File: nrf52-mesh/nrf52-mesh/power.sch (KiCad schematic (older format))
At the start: 8 parts

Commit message: continue nRF52 power
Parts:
- added C? (x6): C, symbol Device:C
- added L? (x2): L, symbol Device:L
- added R? (x6): R, symbol Device:R
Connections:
- net +3V3: now also C?.1, L?.1, R?.1
- net GND: now also U?.2 (GND), U?.2 (GND), C?.2, C?.2, C?.2, C?.2, C?.2, C?.2, R?.2, R?.2, R?.2
- net at U?.1 (EN): now also R?.1, R?.2
- net at U?.3 (PH): now also L?.2
- net +15V: now reaches U?.4 (VIN)
- net +15V: now also C?.1, C?.1, R?.1
- net at U?.5 (FB): now also R?.1, R?.2 (x2)
- net +5V: now reaches U?.1 (EN)
- net +5V: now also U?.4 (VIN), C?.1, C?.1, C?.1, L?.1, R?.1
- net at U?.3 (SW): now also L?.2
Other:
- moved on the sheet: U?

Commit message: next portion
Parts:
- removed U?: CP2102N-A01-GQFN24, Package_DFN_QFN:QFN-24-1EP_4x4mm_P0.5mm_EP2.6x2.6mm, symbol Interface_USB:CP2102N-A01-GQFN24
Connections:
- net GND: now also U?.6 (GND)
- net LEDREGEN: now reaches U?.3 (EN)
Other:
- moved on the sheet: U?
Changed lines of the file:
@@
 $Descr A4 11693 8268
 encoding utf-8
-Sheet 2 7
+Sheet 2 8
 Title ""
 Date ""
@@
 	5400 3450 5400 650
 $Comp
-L Interface_USB:CP2102N-A01-GQFN24 U?
-U 1 1 5E5187FA
-P 5700 5000
-F 0 "U?" H 5700 6081 50  0000 C CNN
-F 1 "CP2102N-A01-GQFN24" H 5700 5990 50  0000 C CNN
-F 2 "Package_DFN_QFN:QFN-24-1EP_4x4mm_P0.5mm_EP2.6x2.6mm" H 6150 4200 50  0001 L CNN
-F 3 "https://www.silabs.com/documents/public/data-sheets/cp2102n-datasheet.pdf" H 5750 3950 50  0001 C CNN
-	1    5700 5000
-	1    0    0    -1
-$EndComp
-$Comp
 L Regulator_Switching:TPS560200 U?
 U 1 1 5E51A6D3
@@
 L kilib:FAN5341 U?
 U 1 1 5E51BD5F
-P 4100 6900
-F 0 "U?" H 4100 7381 50  0000 C CNN
-F 1 "FAN5341" H 4100 7290 50  0000 C CNN
-F 2 "kifootp:FAN5341" H 4150 6650 50  0001 L CNN
-F 3 "" H 4100 6900 50  0001 C CNN
-	1    4100 6900
+P 4800 5400
+F 0 "U?" H 4800 5881 50  0000 C CNN
+F 1 "FAN5341" H 4800 5790 50  0000 C CNN
+F 2 "kifootp:FAN5341" H 4850 5150 50  0001 L CNN
+F 3 "" H 4800 5400 50  0001 C CNN
+	1    4800 5400
 	1    0    0    -1
 $EndComp
@@
 Wire Wire Line
 	3150 6650 3200 6650
+Text GLabel 3650 5400 0    50   Input ~ 0
+LEDREGEN
+Wire Wire Line
+	3650 5400 4400 5400
+$Comp
+L power:GND #PWR?
+U 1 1 5E59FA50
+P 4800 6050
+F 0 "#PWR?" H 4800 5800 50  0001 C CNN
+F 1 "GND" H 4805 5877 50  0000 C CNN
+F 2 "" H 4800 6050 50  0001 C CNN
+F 3 "" H 4800 6050 50  0001 C CNN
+	1    4800 6050
+	1    0    0    -1
+$EndComp
+Wire Wire Line
+	4800 5700 4800 6050
 $EndSCHEMATC

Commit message: next portion
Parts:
- added C? (x2): C, symbol pspice:C
- added L?: L, symbol Device:L
- added R? (x2): R, symbol Device:R
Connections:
- net +3V3: now also U?.2 (VIN), C?.1, L?.1, R?.1
- net +5V: now also U?.5 (BAT)
- net GND: now also C?.2, C?.2, R?.2
- net CHARGE: now reaches U?.3 (CHG#)
- net CHARGE: now also R?.2
- net LEDIN: now reaches U?.1 (VOUT)
- net LEDIN: now also C?.1
- net LEDOUT: now reaches U?.4 (FB)
- net LEDOUT: now also R?.1
- net at U?.5 (SW): now also L?.2
- no-connect marks 0 -> 1
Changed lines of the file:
@@
 Wire Wire Line
 	4800 5700 4800 6050
+$Comp
+L pspice:C C?
+U 1 1 5E5B5AAA
+P 5900 5900
+F 0 "C?" H 6078 5946 50  0000 L CNN
+F 1 "C" H 6078 5855 50  0000 L CNN
+F 2 "" H 5900 5900 50  0001 C CNN
+F 3 "~" H 5900 5900 50  0001 C CNN
+	1    5900 5900
+	1    0    0    -1
+$EndComp
+$Comp
+L Device:R R?
+U 1 1 5E5B6411
+P 5450 5800
+F 0 "R?" H 5520 5846 50  0000 L CNN
+F 1 "R" H 5520 5755 50  0000 L CNN
+F 2 "" V 5380 5800 50  0001 C CNN
+F 3 "~" H 5450 5800 50  0001 C CNN
+	1    5450 5800
+	1    0    0    -1
+$EndComp
+Text GLabel 6200 5400 2    50   Input ~ 0
+LEDIN
+Text GLabel 6200 5500 2    50   Input ~ 0
+LEDOUT
+Wire Wire Line
+	5200 5500 5450 5500
+Wire Wire Line
+	6200 5400 5900 5400
+Wire Wire Line
+	5450 5500 5450 5650
+Connection ~ 5450 5500
+$Comp
+L power:GND #PWR?
+U 1 1 5E5C1EAB
+P 5450 6300
+F 0 "#PWR?" H 5450 6050 50  0001 C CNN
+F 1 "GND" H 5455 6127 50  0000 C CNN
+F 2 "" H 5450 6300 50  0001 C CNN
+F 3 "" H 5450 6300 50  0001 C CNN
+	1    5450 6300
+	1    0    0    -1
+$EndComp
+Wire Wire Line
+	5450 5950 5450 6300
+$Comp
+L power:GND #PWR?
+U 1 1 5E5C3E72
+P 5900 6500
+F 0 "#PWR?" H 5900 6250 50  0001 C CNN
+F 1 "GND" H 5905 6327 50  0000 C CNN
+F 2 "" H 5900 6500 50  0001 C CNN
+F 3 "" H 5900 6500 50  0001 C CNN
+	1    5900 6500
+	1    0    0    -1
+$EndComp
+Wire Wire Line
+	5900 6150 5900 6500
+Wire Wire Line
+	5450 5500 6200 5500
+Wire Wire Line
+	5900 5650 5900 5400
+Connection ~ 5900 5400
+Wire Wire Line
+	5900 5400 5200 5400
+$Comp
+L pspice:C C?
+U 1 1 5E5C88CC
+P 4100 4500
+F 0 "C?" H 4278 4546 50  0000 L CNN
+F 1 "C" H 4278 4455 50  0000 L CNN
+F 2 "" H 4100 4500 50  0001 C CNN
+F 3 "~" H 4100 4500 50  0001 C CNN
+	1    4100 4500
+	1    0    0    -1
+$EndComp
+$Comp
+L Device:L L?
+U 1 1 5E5C902A
+P 5450 4850
+F 0 "L?" H 5503 4896 50  0000 L CNN
+F 1 "L" H 5503 4805 50  0000 L CNN
+F 2 "" H 5450 4850 50  0001 C CNN
+F 3 "~" H 5450 4850 50  0001 C CNN
+	1    5450 4850
+	1    0    0    -1
+$EndComp
+$Comp
+L power:GND #PWR?
+U 1 1 5E5C97A4
+P 4100 5100
+F 0 "#PWR?" H 4100 4850 50  0001 C CNN
+F 1 "GND" H 4105 4927 50  0000 C CNN
+F 2 "" H 4100 5100 50  0001 C CNN
+F 3 "" H 4100 5100 50  0001 C CNN
+	1    4100 5100
+	1    0    0    -1
+$EndComp
+Wire Wire Line
+	4100 4750 4100 5100
+Wire Wire Line
+	4800 5100 4800 4300
+Wire Wire Line
+	4800 3900 4100 3900
+Wire Wire Line
+	4100 3900 4100 4250
+Wire Wire Line
+	5450 4700 5450 4300
+Wire Wire Line
+	5450 4300 4800 4300
+Connection ~ 4800 4300
+Wire Wire Line
+	4800 4300 4800 3900
+$Comp
+L power:+3V3 #PWR?
+U 1 1 5E5D1C7A
+P 4800 3700
+AR Path="/5E5D1C7A" Ref="#PWR?"  Part="1"
+AR Path="/5E4CCB9A/5E5D1C7A" Ref="#PWR?"  Part="1"
+F 0 "#PWR?" H 4800 3550 50  0001 C CNN
+F 1 "+3V3" H 4815 3873 50  0000 C CNN
+F 2 "" H 4800 3700 50  0001 C CNN
+F 3 "" H 4800 3700 50  0001 C CNN
+	1    4800 3700
+	1    0    0    -1
+$EndComp
+Wire Wire Line
+	4800 3700 4800 3900
+Connection ~ 4800 3900
+Wire Wire Line
+	5200 5300 5450 5300
+Wire Wire Line
+	5450 5300 5450 5000
+$Comp
+L power:+5V #PWR?
+U 1 1 5E5DDB7A
+P 2950 4050
+F 0 "#PWR?" H 2950 3900 50  0001 C CNN
+F 1 "+5V" H 2965 4223 50  0000 C CNN
+F 2 "" H 2950 4050 50  0001 C CNN
+F 3 "" H 2950 4050 50  0001 C CNN
+	1    2950 4050
+	1    0    0    -1
+$EndComp
+Wire Wire Line
+	2200 4500 2950 4500
+Wire Wire Line
+	2950 4500 2950 4050
+$Comp
+L power:+3V3 #PWR?
+U 1 1 5E5E538B
+P 3350 4050
+AR Path="/5E5E538B" Ref="#PWR?"  Part="1"
+AR Path="/5E4CCB9A/5E5E538B" Ref="#PWR?"  Part="1"
+F 0 "#PWR?" H 3350 3900 50  0001 C CNN
+F 1 "+3V3" H 3365 4223 50  0000 C CNN
+F 2 "" H 3350 4050 50  0001 C CNN
+F 3 "" H 3350 4050 50  0001 C CNN
+	1    3350 4050
+	1    0    0    -1
+$EndComp
+$Comp
+L Device:R R?
+U 1 1 5E5E8405
+P 3350 4450
+F 0 "R?" H 3420 4496 50  0000 L CNN
+F 1 "R" H 3420 4405 50  0000 L CNN
+F 2 "" V 3280 4450 50  0001 C CNN
+F 3 "~" H 3350 4450 50  0001 C CNN
+	1    3350 4450
+	1    0    0    -1
+$EndComp
+Wire Wire Line
+	3350 4050 3350 4300
+Wire Wire Line
+	3350 4800 3350 4600
+Text GLabel 2950 5050 2    50   Input ~ 0
+CHARGE
+Wire Wire Line
+	2500 4800 2500 5050
+Wire Wire Line
+	2500 5050 2950 5050
+Wire Wire Line
+	2200 4800 2500 4800
+Connection ~ 2500 4800
+Wire Wire Line
+	2500 4800 3350 4800
+NoConn ~ 1400 4800
 $EndSCHEMATC

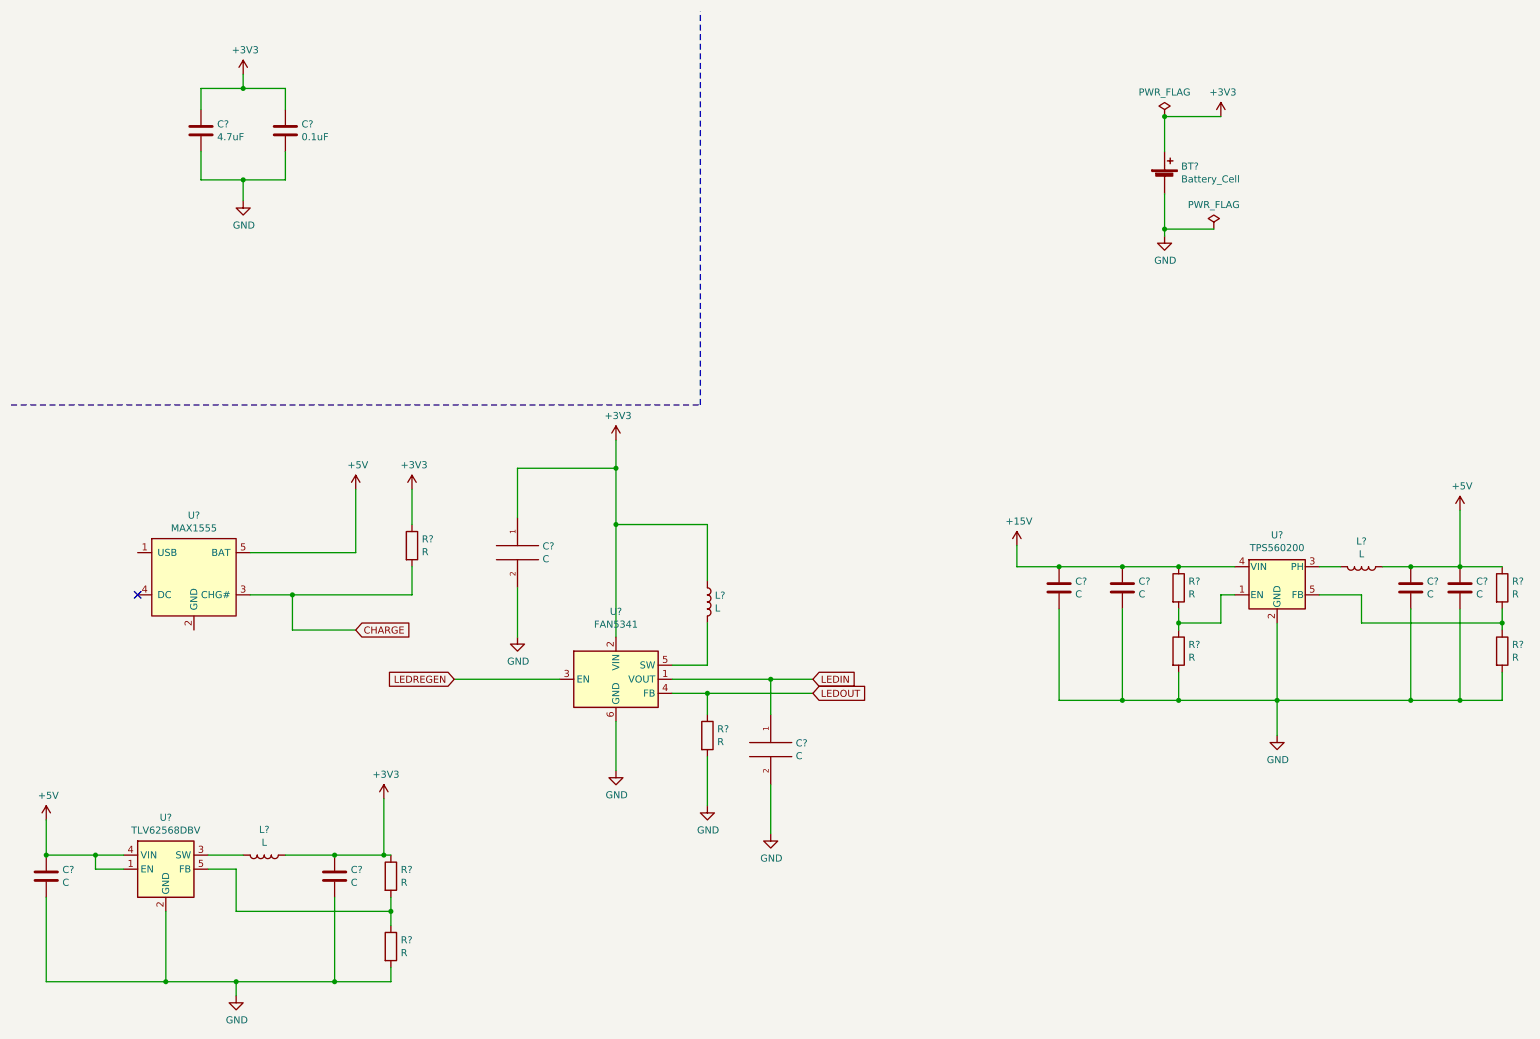
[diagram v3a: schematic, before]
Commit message: CP2102N + MAX1555 + FAN5341 + TPS560200 + TLV62568
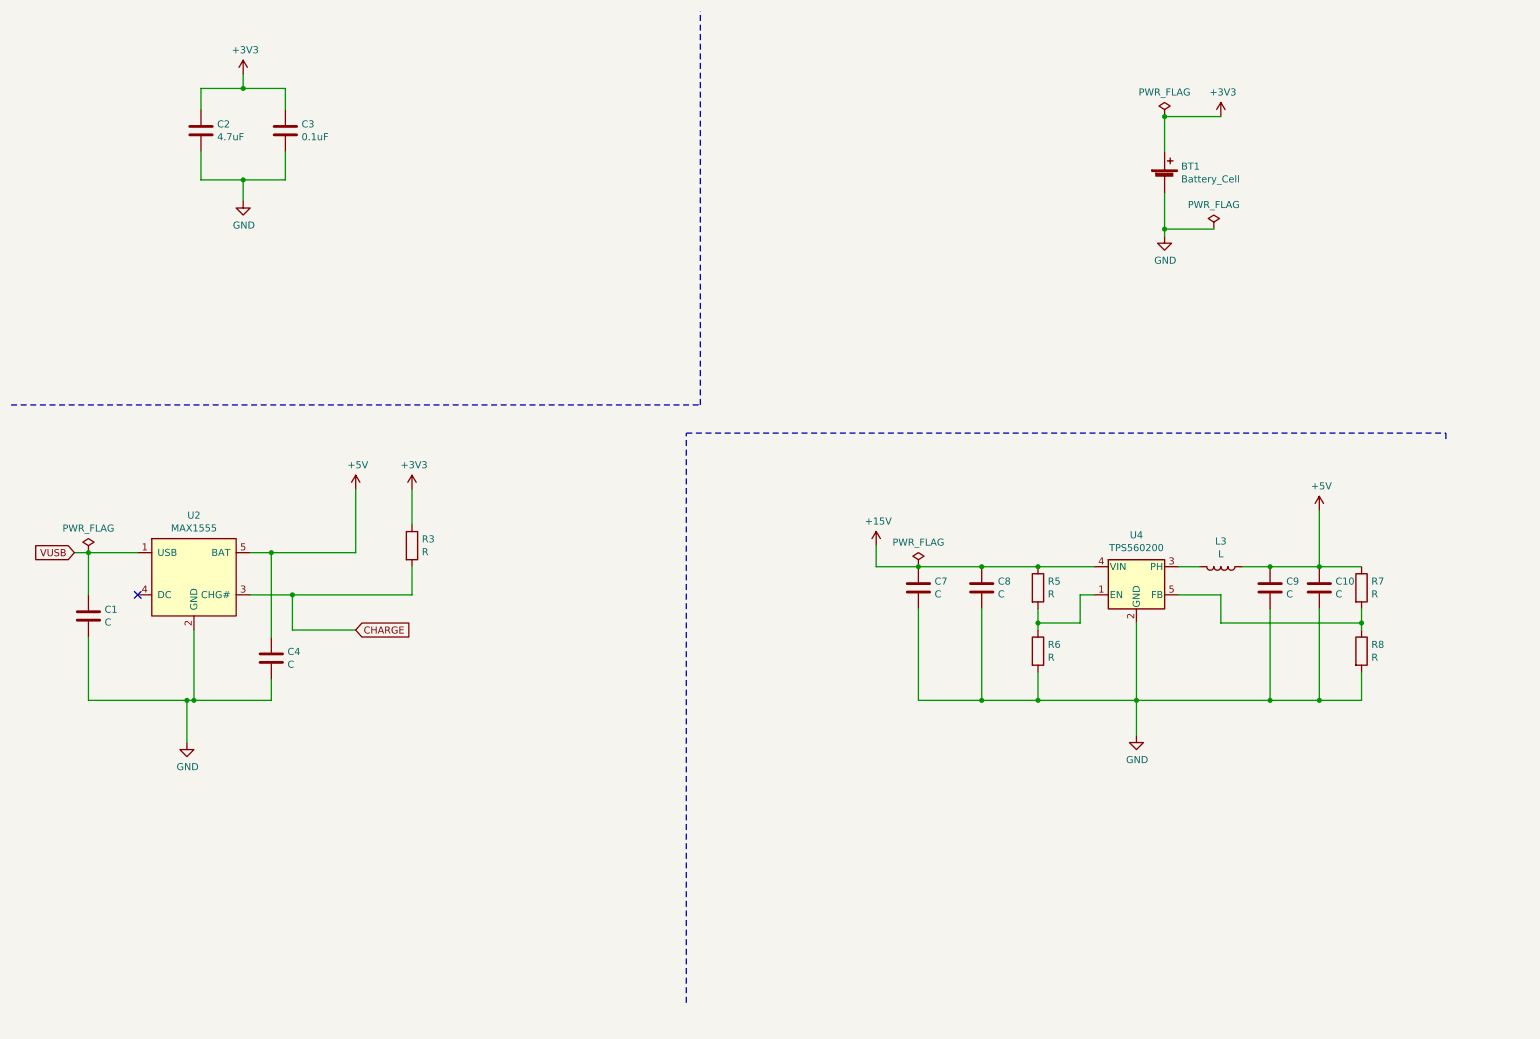
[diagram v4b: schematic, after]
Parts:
- removed C? (x2): C, symbol Device:C
- removed C? (x2): C, symbol pspice:C
- removed L? (x2): L, symbol Device:L
- removed R? (x3): R, symbol Device:R
- removed U?: TLV62568DBV, Package_TO_SOT_SMD:SOT-23-5, symbol Regulator_Switching:TLV62568DBV
- removed U?: FAN5341, kifootp:FAN5341, symbol kilib:FAN5341
- added C1, C4: C, symbol Device:C
- gave numbers to parts that had none: 15
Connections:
- net +5V: now also C4.2
- net GND: now also U2.2 (GND), C1.2, C4.1
- net VUSB: now reaches U2.1 (USB)
- net VUSB: now also C1.1
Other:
- moved on the sheet: C10, C7, C8, C9, L3, R5, R6, R7, R8, U4

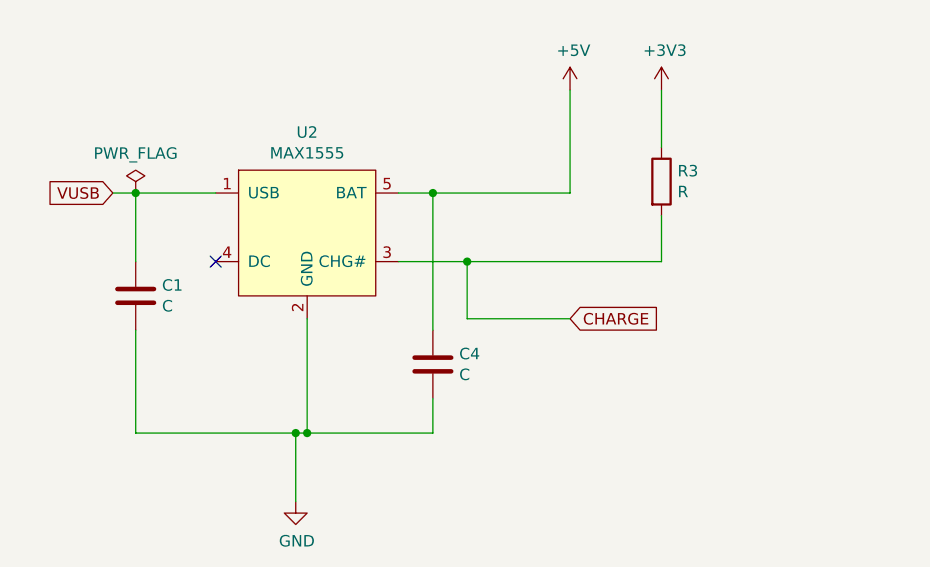
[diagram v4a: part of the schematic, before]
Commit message: CP2102N + MAX1555 + FAN5341 + TPS560200 + TLV62568
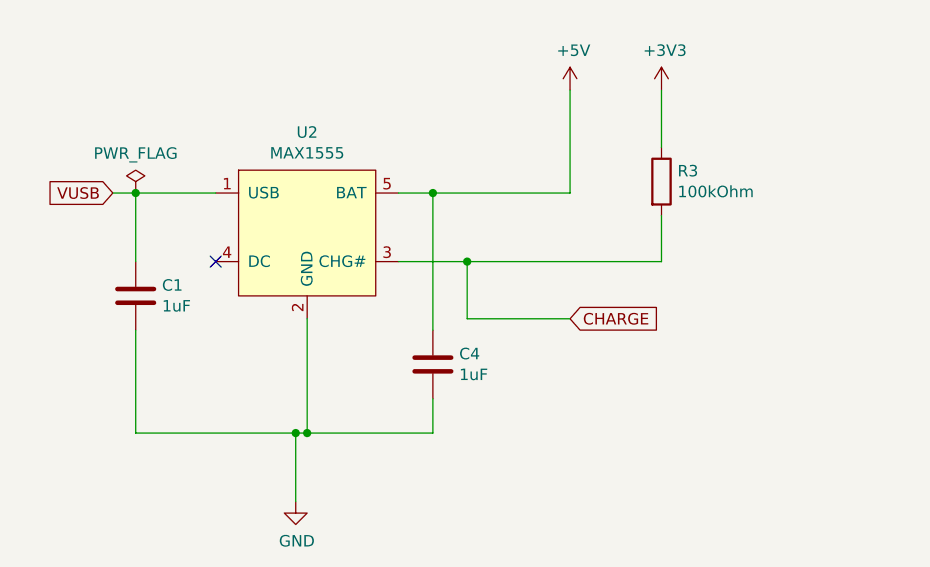
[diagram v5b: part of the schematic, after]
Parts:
- C1, C4: value C -> 1uF
- R3: value R -> 100kOhm
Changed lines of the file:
@@
 P 3350 4450
 F 0 "R3" H 3420 4496 50  0000 L CNN
-F 1 "R" H 3420 4405 50  0000 L CNN
+F 1 "100kOhm" H 3420 4405 50  0000 L CNN
 F 2 "" V 3280 4450 50  0001 C CNN
 F 3 "~" H 3350 4450 50  0001 C CNN
@@
 P 1050 4950
 F 0 "C1" H 1165 4996 50  0000 L CNN
-F 1 "C" H 1165 4905 50  0000 L CNN
+F 1 "1uF" H 1165 4905 50  0000 L CNN
 F 2 "" H 1088 4800 50  0001 C CNN
 F 3 "~" H 1050 4950 50  0001 C CNN
@@
 P 2350 5250
 F 0 "C4" H 2235 5204 50  0000 R CNN
-F 1 "C" H 2235 5295 50  0000 R CNN
+F 1 "1uF" H 2235 5295 50  0000 R CNN
 F 2 "" H 2388 5100 50  0001 C CNN
 F 3 "~" H 2350 5250 50  0001 C CNN

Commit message: CP2102N + MAX1555 + FAN5341 + TPS560200 + TLV62568
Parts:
- C1, C4, R3: footprint (none) -> Resistor_SMD:R_0402_1005Metric
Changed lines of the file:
@@
 F 0 "R3" H 3420 4496 50  0000 L CNN
 F 1 "100kOhm" H 3420 4405 50  0000 L CNN
-F 2 "" V 3280 4450 50  0001 C CNN
+F 2 "Resistor_SMD:R_0402_1005Metric" V 3280 4450 50  0001 C CNN
 F 3 "~" H 3350 4450 50  0001 C CNN
 	1    3350 4450
@@
 F 0 "C1" H 1165 4996 50  0000 L CNN
 F 1 "1uF" H 1165 4905 50  0000 L CNN
-F 2 "" H 1088 4800 50  0001 C CNN
+F 2 "Resistor_SMD:R_0402_1005Metric" H 1088 4800 50  0001 C CNN
 F 3 "~" H 1050 4950 50  0001 C CNN
 	1    1050 4950
@@
 F 0 "C4" H 2235 5204 50  0000 R CNN
 F 1 "1uF" H 2235 5295 50  0000 R CNN
-F 2 "" H 2388 5100 50  0001 C CNN
+F 2 "Resistor_SMD:R_0402_1005Metric" H 2388 5100 50  0001 C CNN
 F 3 "~" H 2350 5250 50  0001 C CNN
 	1    2350 5250
